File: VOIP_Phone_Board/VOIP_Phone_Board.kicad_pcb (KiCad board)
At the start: 2 copper layers, 65 x 56 mm, 53 parts, among them J1 Headset, J2 Display, J3 KeypadConnector, J4 Hook, J5 Speaker, J6 Microphone, J7 Control Buttons, P1 Conn_02x20_Odd_Even, U1 PCM5102, U2 PCM1808PW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

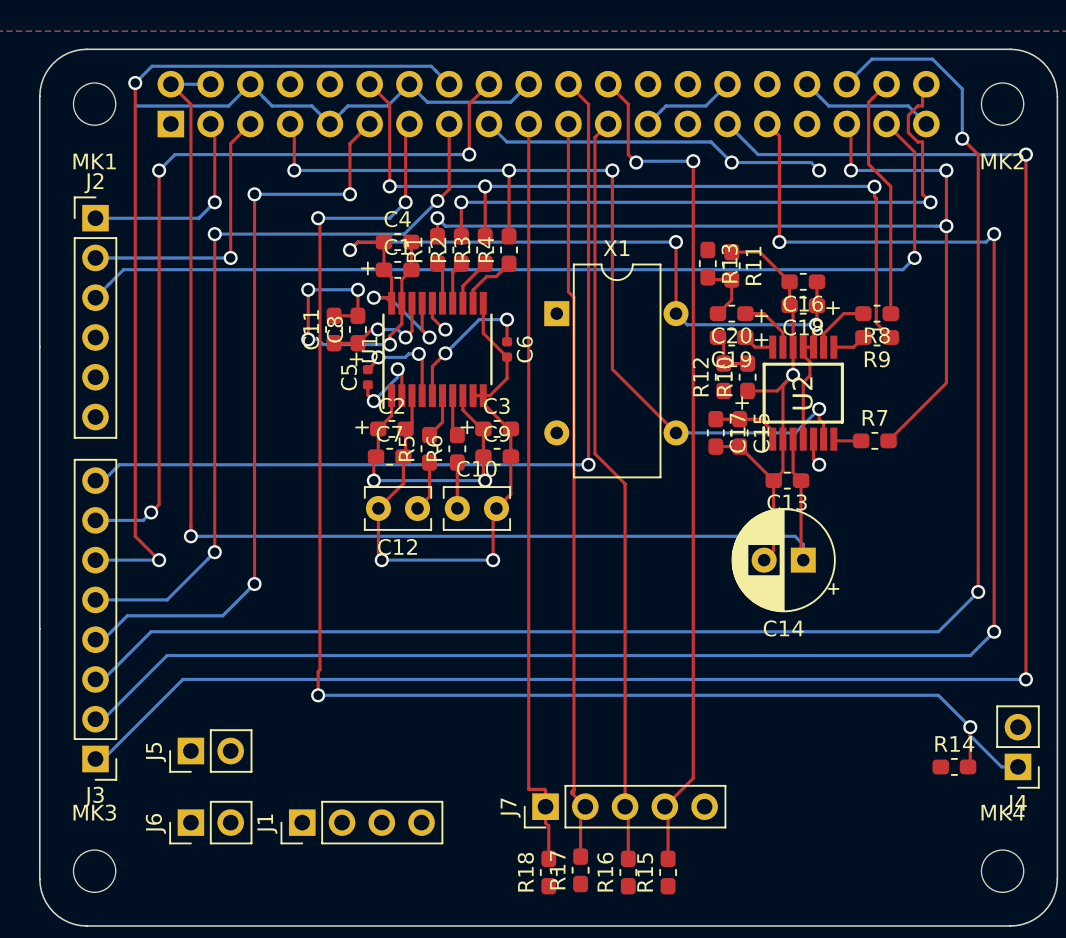
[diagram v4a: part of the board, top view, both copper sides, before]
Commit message: MAX98357A Version.
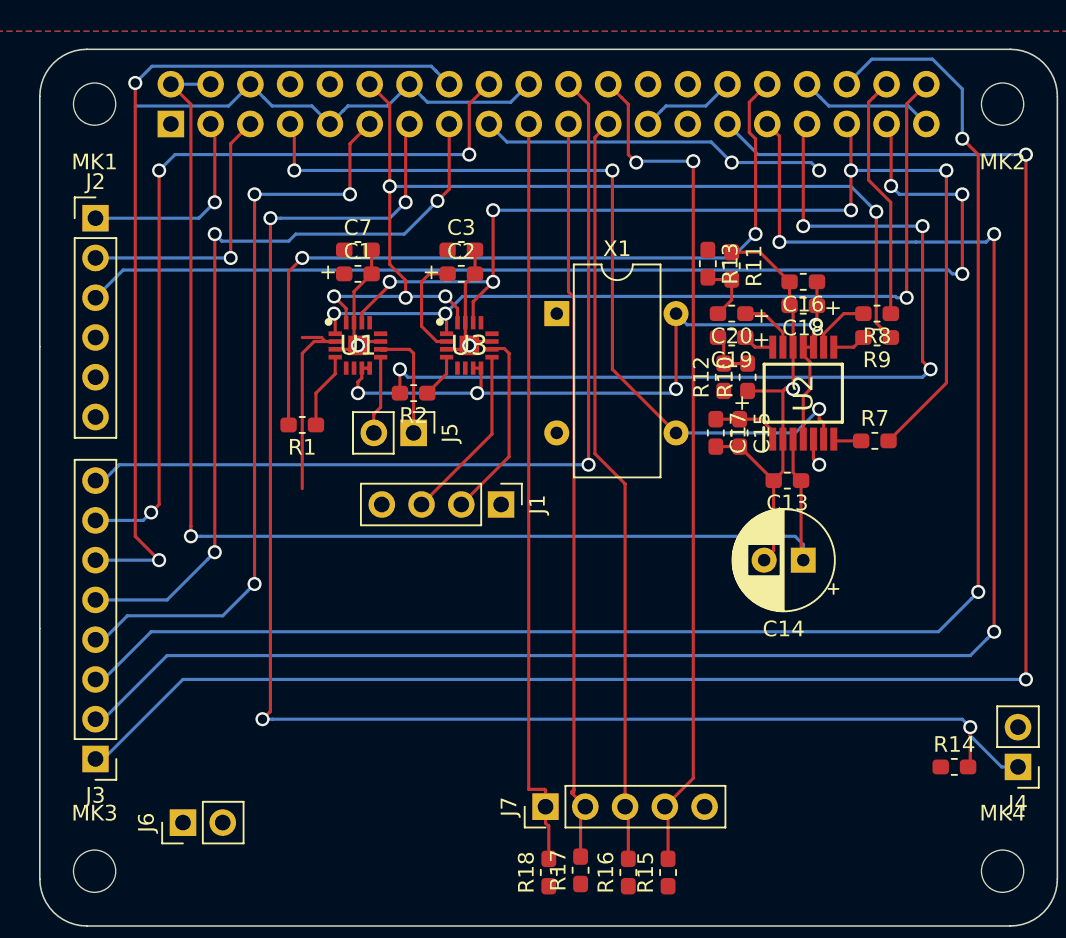
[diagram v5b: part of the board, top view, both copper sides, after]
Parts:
- removed C10, C12: 2200pf, Capacitor_THT:C_Rect_L4.0mm_W2.5mm_P2.50mm
- removed C11, C4, C9: .1uf, Capacitor_SMD:C_0603_1608Metric_Pad1.05x0.95mm_HandSolder
- removed C5, C6: 2.2uf, Capacitor_SMD:C_0402_1005Metric
- removed C8: 10uf, VOIP_Phone_Board:CP_0603_1608Metric_Pad1.05x0.95mm_HandSolder
- removed R3, R4: 51, Resistor_SMD:R_0603_1608Metric_Pad1.05x0.95mm_HandSolder
- removed R5, R6: 470, Resistor_SMD:R_0603_1608Metric_Pad1.05x0.95mm_HandSolder
- added U3: MAX98357AETE+T, QFN50P300X300X80-17N, F.Cu at (227.4, 112.9)
- C3: value 10uf -> .1uf; footprint VOIP_Phone_Board:CP_0603_1608Metric_Pad1.05x0.95mm_HandSolder -> Capacitor_SMD:C_0603_1608Metric_Pad1.05x0.95mm_HandSolder
- R1, R2: value 51 -> 634K
- U1: value PCM5102 -> MAX98357AETE+T; footprint Package_SO:TSSOP-20_4.4x6.5mm_P0.65mm -> QFN50P300X300X80-17N
- moved J5 24.8 mm to (223.9, 118.5), turned to 270 degrees
- moved J1 24.0 mm to (229.5, 123.1), turned to 270 degrees
- moved R1 14.1 mm to (216.8, 118.0), turned to 180 degrees
- moved C7 13.4 mm to (220.3, 106.8)
- moved C3 11.7 mm to (226.9, 106.8)
- moved C2 10.9 mm to (226.9, 108.3)
- moved R2 9.64 mm to (223.9, 116.0), turned to 180 degrees
- moved U1 5.09 mm to (220.3, 112.9), turned to 0 degrees
- moved C1 2.55 mm to (220.3, 108.3)
- moved J6 0.51 mm to (209.1, 143.4)
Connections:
- R1 pad 2: /DAP4_FS -> /GPIO12(PWM0)
- R2 pad 2: /DAP4_DOUT -> /GPIO13(PWM1)
- U1 pad 1: +3V3 -> /DAP4_DOUT
- U1 pad 10: GND -> /Audio Subsystem/SpeakerA
- U1 pad 14: Net-(R2-Pad1) -> /DAP4_FS
- U1 pad 15: Net-(R1-Pad1) -> GND
- U1 pad 16: GND -> /DAP4_SCLK
- U1 pad 17: +3V3 -> GND
- U1 pad 2: Net-(C5-Pad1) -> +3V3
- U1 pad 4: Net-(C5-Pad2) -> Net-(R1-Pad1)
- U1 pad 7: Net-(R6-Pad2) -> +3V3
- U1 pad 9: GND -> /Audio Subsystem/SpeakerB
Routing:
- net /GPIO13(PWM1): track 0.00 -> 59.4 mm, vias 0 -> 4
- net /GPIO12(PWM0): track 0.00 -> 51.2 mm, vias 0 -> 2
- net GND: track 139.0 -> 95.3 mm, vias 9 -> 4
- net /DAP4_SCLK: track 51.3 -> 65.9 mm, vias 3 -> 5
- net /DAP4_DOUT: track 41.1 -> 53.9 mm, vias 2 -> 3
- net /Audio Subsystem/SPKR_A(Red): track 0.00 -> 12.2 mm
- net /Audio Subsystem/SPKR_B(Green): track 0.00 -> 11.3 mm
- net +3V3: track 102.6 -> 92.7 mm, vias 9 -> 6
- net Net-(U1-Pad5): track 9.29 -> 0.00 mm, vias 2 -> 0
- net /DAP4_FS: track 61.9 -> 71.0 mm, vias 4 -> 6
- net /GPIO27(GEN2): track 91.2 -> 98.8 mm
- net Net-(C11-Pad1): track 7.50 -> 0.00 mm, vias 2 -> 0
- net /GPIO26: track 62.7 -> 70.1 mm, vias 1 -> 3
- net /Audio Subsystem/SpeakerA: track 0.00 -> 7.33 mm
- net Net-(C5-Pad2): track 6.49 -> 0.00 mm, vias 2 -> 0
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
